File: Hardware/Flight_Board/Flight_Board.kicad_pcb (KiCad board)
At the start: 4 copper layers, 31.8 x 82.6 mm, 88 parts, among them J1 Conn_01x04, J2 Conn_01x08, J3 Conn_01x04, J4 Conn_01x06, J5 MEM2067-02-180-00-A_REVB, U1 FT5HN, U2 STM32F411RCTx, U3 ADXL375, U4 BMP390, U5 FGPMMOPA6H, U6 BMI323, U7 AP2205-33Y-13, U8 TPS274160A, U9 LR62E

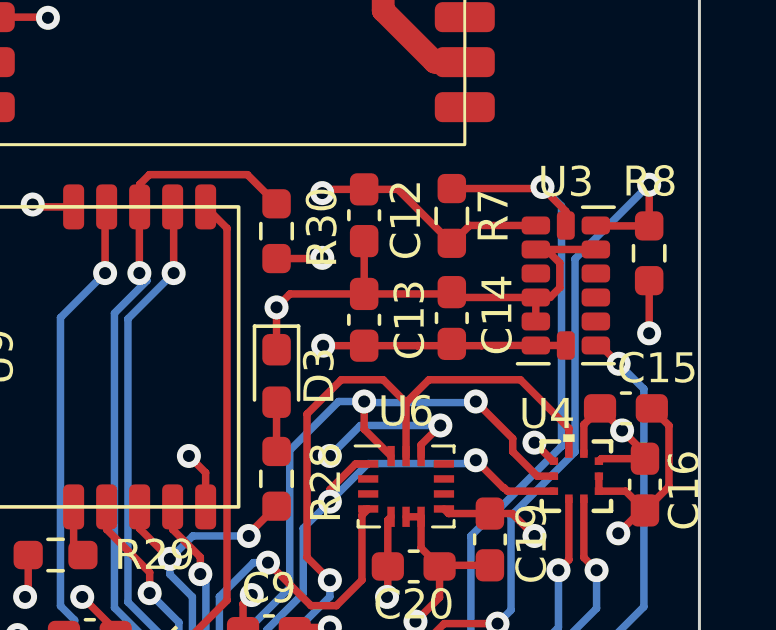
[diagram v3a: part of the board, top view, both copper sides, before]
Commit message: fix track stub and generate first gerbers
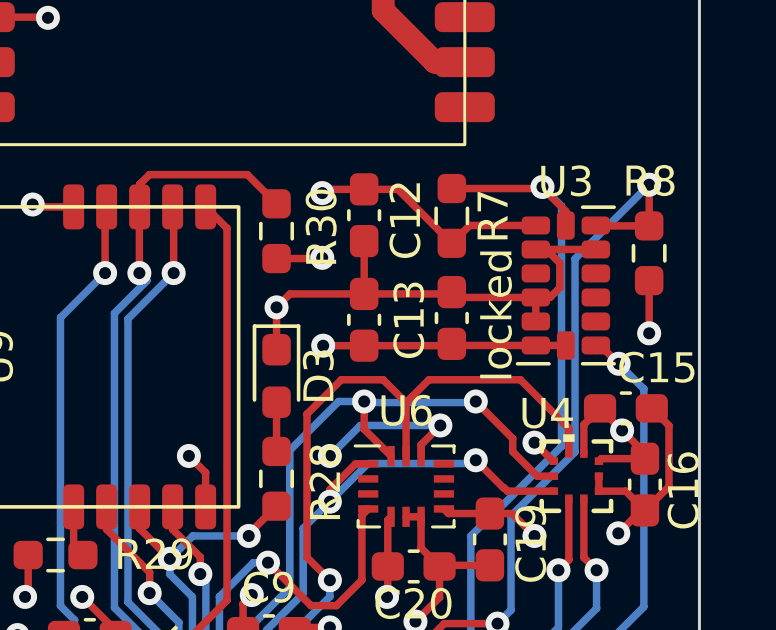
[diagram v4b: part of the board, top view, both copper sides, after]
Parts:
- renumbered C14 to locked
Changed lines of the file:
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@@
     (pad_to_mask_clearance 0)
     (pcbplotparams
-      (layerselection 0x00010fc_ffffffff)
+      (layerselection 0x00010f0_ffffffff)
       (plot_on_all_layers_selection 0x0000000_00000000)
       (disableapertmacros false)
-      (usegerberextensions false)
-      (usegerberattributes true)
+      (usegerberextensions true)
+      (usegerberattributes false)
       (usegerberadvancedattributes true)
       (creategerberjobfile true)
@@
       (plotinvisibletext false)
       (sketchpadsonfab false)
-      (subtractmaskfromsilk false)
+      (subtractmaskfromsilk true)
       (outputformat 1)
       (mirror false)
-      (drillshape 1)
+      (drillshape 0)
       (scaleselection 1)
-      (outputdirectory "")
+      (outputdirectory "gerbers")
     )
   )
@@
     (property "ki_keywords" "cap capacitor")
     (attr smd)
-    (fp_text reference "C14" (at 0.1005 1.524 90) (layer "F.SilkS")
+    (fp_text reference locked "C14" (at 0.1005 1.524 90) (layer "F.SilkS")
         (effects (font (size 1 1) (thickness 0.15)))
     )
@@
   (segment (start 148.1825 112.8988) (end 149.133819 111.947481) (width 0.25) (layer "F.Cu") (net 1))
   (segment (start 148.1825 115.062) (end 148.1825 115.9775) (width 0.25) (layer "F.Cu") (net 1))
+  (segment (start 160.073 86.995) (end 160.02 86.942) (width 0.25) (layer "F.Cu") (net 1))
   (segment (start 155.702 81.915) (end 155.826 81.791) (width 0.25) (layer "F.Cu") (net 1))
   (segment (start 155.826 81.791) (end 157.099 81.791) (width 0.25) (layer "F.Cu") (net 1))
@@
   (segment (start 151.815 92.376) (end 151.815 91.236) (width 0.25) (layer "F.Cu") (net 1))
   (segment (start 158.2155 107.7002) (end 158.2155 112.014) (width 0.25) (layer "F.Cu") (net 1))
+  (segment (start 160.02 86.942) (end 159.96 87.002) (width 0.25) (layer "F.Cu") (net 1))
   (segment (start 143.4835 108.405412) (end 143.4835 109.474) (width 0.25) (layer "F.Cu") (net 1))
   (segment (start 139.446 73.533) (end 138.684 74.295) (width 0.25) (layer "F.Cu") (net 1))
-  (segment (start 161.0095 87.002) (end 161.0165 86.995) (width 0.25) (layer "F.Cu") (net 1))
   (segment (start 164.423063 90.6017) (end 164.423063 89.629937) (width 0.25) (layer "F.Cu") (net 1))
   (segment (start 137.668 93.853) (end 137.541 93.726) (width 0.25) (layer "F.Cu") (net 1))
@@
   (segment (start 160.52525 137.493) (end 161.80075 137.493) (width 0.762) (layer "F.Cu") (net 1))
   (segment (start 163.83 122.301) (end 163.4725 122.6585) (width 0.25) (layer "F.Cu") (net 1))
-  (segment (start 158.8825 86.9965) (end 158.877 87.002) (width 0.25) (layer "F.Cu") (net 1))
   (segment (start 153.0615 95.605206) (end 153.0615 96.52) (width 0.25) (layer "F.Cu") (net 1))
-  (segment (start 158.877 87.002) (end 161.0095 87.002) (width 0.25) (layer "F.Cu") (net 1))
   (segment (start 161.29 92.5975) (end 159.912 92.5975) (width 0.25) (layer "F.Cu") (net 1))
   (segment (start 157.8875 94.361) (end 157.8875 95.3505) (width 0.25) (layer "F.Cu") (net 1))
@@
   (segment (start 153.352853 95.313853) (end 153.0615 95.605206) (width 0.25) (layer "F.Cu") (net 1))
   (segment (start 148.8175 98.3022) (end 149.133819 98.618519) (width 0.25) (layer "F.Cu") (net 1))
+  (segment (start 159.96 87.002) (end 157.099 87.002) (width 0.25) (layer "F.Cu") (net 1))
   (segment (start 154.2815 128.8815) (end 154.2815 128.27) (width 0.25) (layer "F.Cu") (net 1))
   (segment (start 159.766 122.428) (end 159.766 123.6715) (width 0.25) (layer "F.Cu") (net 1))
   (segment (start 153.416 115.7205) (end 150.114 115.7205) (width 0.25) (layer "F.Cu") (net 1))
   (segment (start 162.8155 87.0005) (end 162.821 86.995) (width 0.25) (layer "F.Cu") (net 1))
-  (segment (start 162.821 86.995) (end 161.0165 86.995) (width 0.25) (layer "F.Cu") (net 1))
   (segment (start 163.4725 122.6585) (end 163.4725 123.698) (width 0.25) (layer "F.Cu") (net 1))
   (segment (start 161.29 92.5975) (end 162.029 92.5975) (width 0.25) (layer "F.Cu") (net 1))
@@
   (segment (start 141.732 104.2905) (end 141.732 106.045) (width 0.25) (layer "F.Cu") (net 1))
   (segment (start 159.94075 136.9085) (end 160.52525 137.493) (width 0.762) (layer "F.Cu") (net 1))
+  (segment (start 162.821 86.995) (end 160.073 86.995) (width 0.25) (layer "F.Cu") (net 1))
   (segment (start 159.94075 136.9085) (end 159.3825 136.9085) (width 0.762) (layer "F.Cu") (net 1))
-  (segment (start 158.877 87.002) (end 157.099 87.002) (width 0.25) (layer "F.Cu") (net 1))
   (via (at 162.7765 93.345) (size 0.8) (drill 0.4) (layers "F.Cu" "B.Cu") (net 1))
   (via (at 155.7325 87.002) (size 0.8) (drill 0.4) (layers "F.Cu" "B.Cu") (net 1))

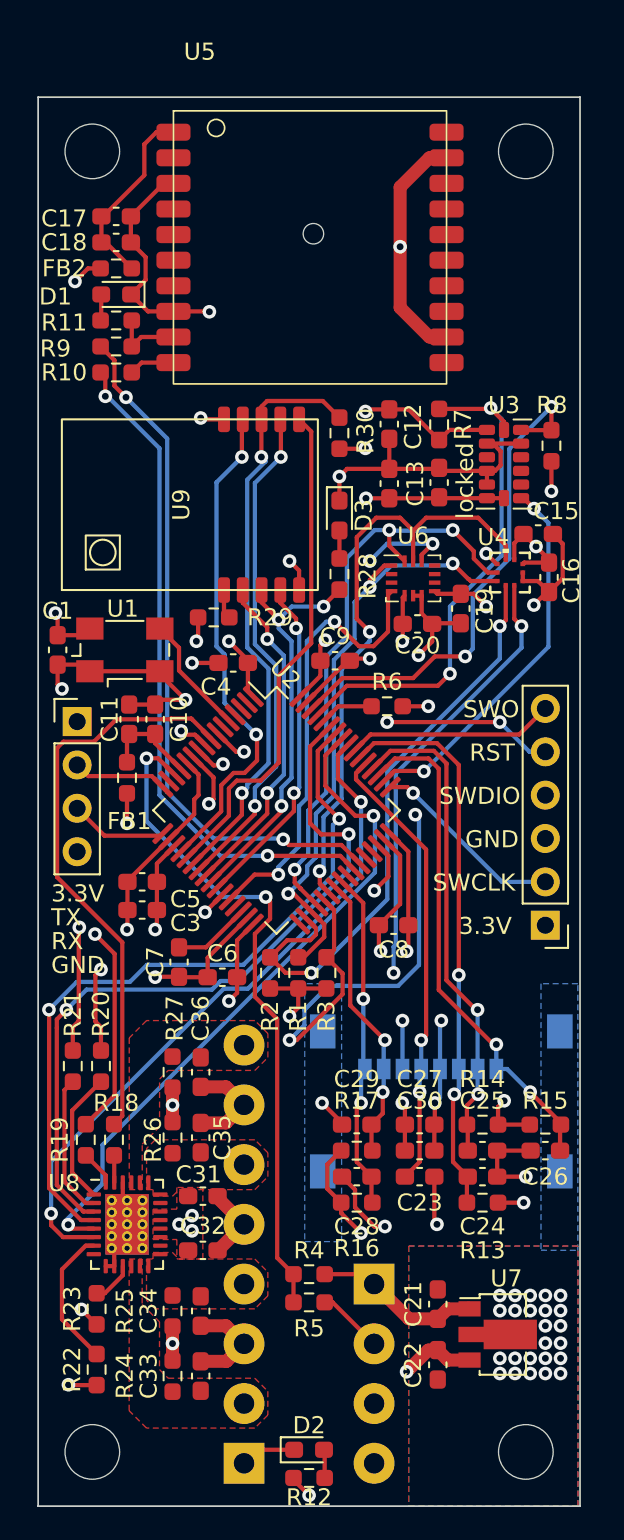
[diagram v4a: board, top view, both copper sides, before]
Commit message: reroute inner traces and tx/rx GPS lines
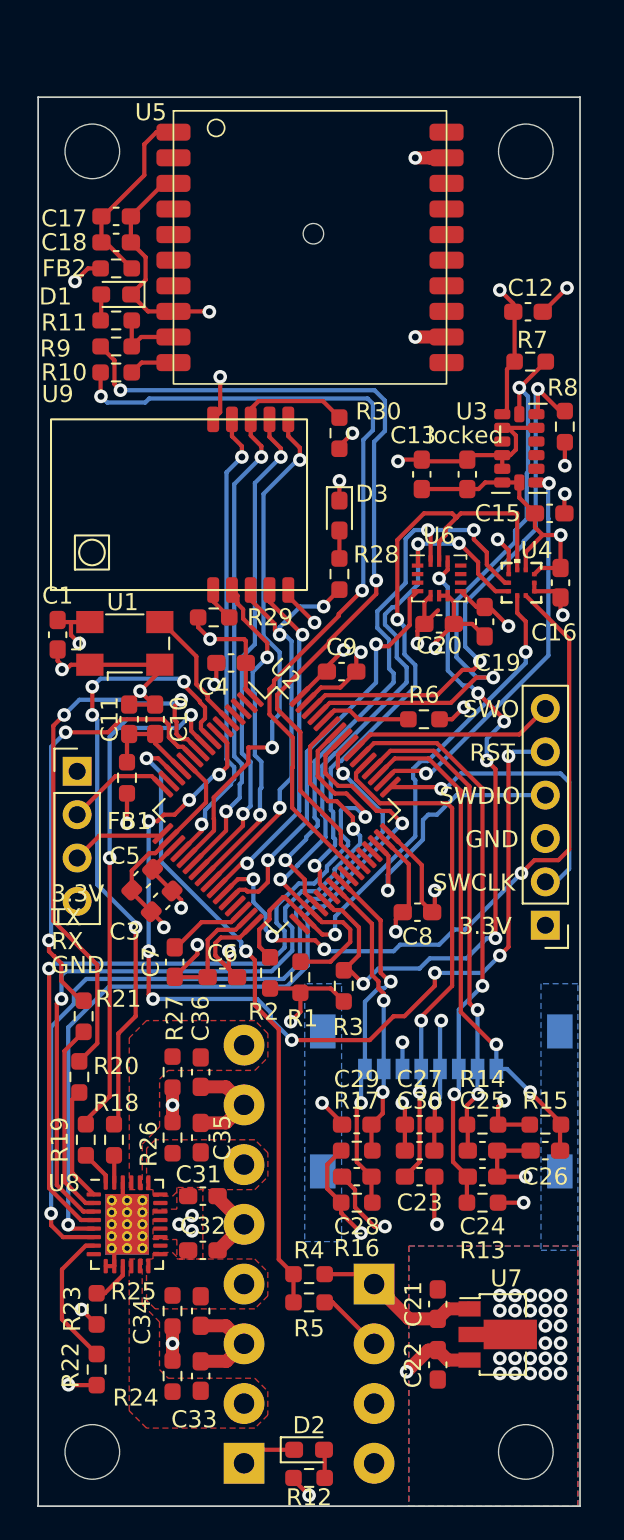
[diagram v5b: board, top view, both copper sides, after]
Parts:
- moved C12 10.5 mm to (165.2, 76.1), turned to 180 degrees
- moved R7 6.48 mm to (165.4, 79.0), turned to 0 degrees
- moved R21 2.99 mm to (139.2, 117.3)
- moved J3 2.91 mm to (138.8, 103.0)
- moved R6 2.29 mm to (159.1, 99.9)
- moved C13 1.98 mm to (159.0, 85.6)
- moved locked 1.72 mm to (161.7, 85.6)
- moved C19 1.60 mm to (162.7, 94.2)
- moved C8 1.59 mm to (158.8, 111.3)
- moved U6 1.52 mm to (160.0, 91.7)
- moved R20 1.42 mm to (138.9, 120.9)
- moved C15 1.38 mm to (166.5, 87.9)
- moved R8 1.37 mm to (167.4, 82.8)
- moved U3 1.29 mm to (164.7, 84.1)
- moved C20 1.27 mm to (160.0, 94.4)
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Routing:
- net /Microcontroller/NRST: track 21.1 -> 56.9 mm, vias 3 -> 9
- net GND: track 157.4 -> 143.7 mm, vias 46 -> 50
- net /Current Switch/EN3: track 22.2 -> 33.4 mm
- net /CS2: track 51.5 -> 40.7 mm, vias 4 -> 6
- net /GPS/RXD: track 39.5 -> 49.6 mm
- net /GPS/TXD: track 40.8 -> 50.8 mm
- net /Current Switch/~{ST3}: track 39.9 -> 47.9 mm
- net +3.3V: track 98.3 -> 106.1 mm, vias 26 -> 24
- net /Current Switch/~{ST4}: track 40.1 -> 47.7 mm
- net /Microcontroller/SWCLK: track 11.4 -> 18.5 mm
- net /Current Switch/~{ST2}: track 43.2 -> 49.9 mm
- net /Barometer/MISO: track 36.1 -> 42.1 mm
- net /Accelerometer/SCL: track 30.6 -> 35.3 mm
- net /Current Switch/EN4: track 22.3 -> 26.2 mm
- net /MicroSD/SDIO_CLK: track 26.7 -> 30.3 mm
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
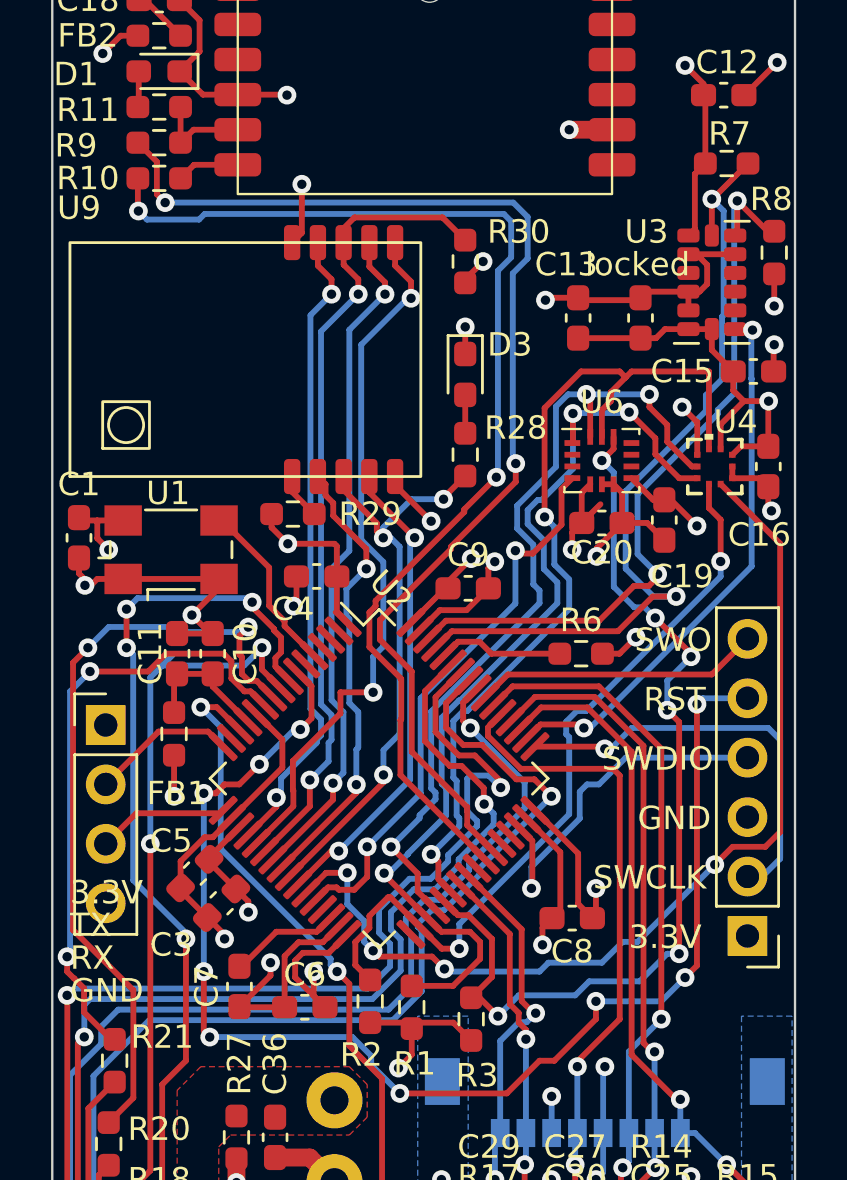
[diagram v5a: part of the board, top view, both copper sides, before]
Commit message: reroute floating traces in radio void
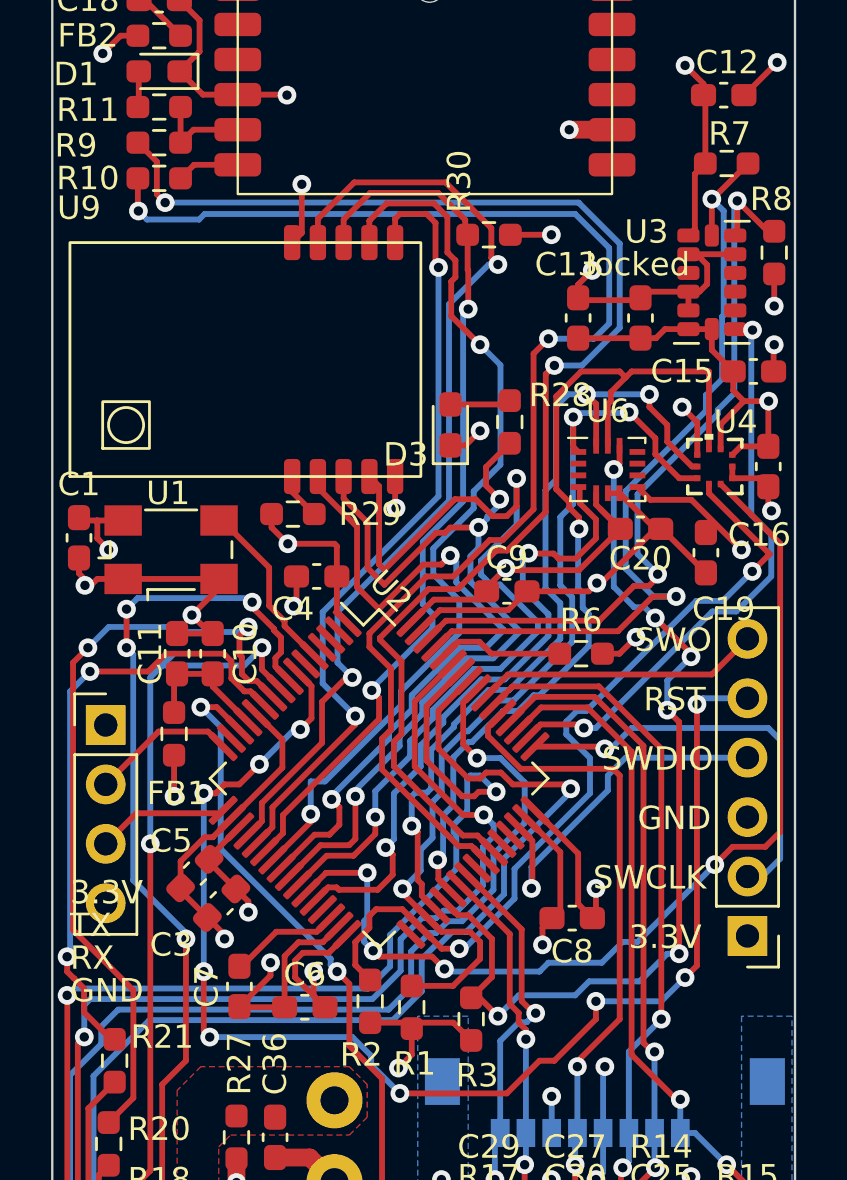
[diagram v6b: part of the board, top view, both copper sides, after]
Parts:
- moved R28 2.36 mm to (156.1, 90.0)
- moved C19 2.26 mm to (164.5, 95.6)
- moved D3 2.25 mm to (153.5, 90.2), turned to 90 degrees
- moved C20 1.67 mm to (161.7, 94.6)
- moved C9 1.66 mm to (156.0, 97.3)
- moved R30 1.53 mm to (155.2, 82.0), turned to 180 degrees
- moved U6 0.46 mm to (160.3, 92.1)
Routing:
- net /LoRa/LORA_DIO1: track 20.5 -> 37.7 mm
- net /LoRa/LORA_NSS: track 27.4 -> 41.3 mm
- net /LoRa/LORA_BUSY: track 25.1 -> 36.4 mm
- net /LoRa/LORA_RST: track 19.5 -> 30.3 mm
- net /LoRa/LORA_MOSI: track 29.1 -> 38.7 mm
- net /GPS/RXD: track 49.6 -> 57.6 mm
- net +3.3V: track 106.1 -> 113.2 mm, vias 24 -> 23
- net /GPS/TXD: track 50.8 -> 57.8 mm
- net GND: track 143.7 -> 150.7 mm, vias 50 -> 49
- net /LoRa/LORA_MISO: track 34.7 -> 38.6 mm
- net /IMU/INT1: track 24.1 -> 27.7 mm
- net /LoRa/LORA_SCK: track 30.5 -> 34.0 mm
- net /CS1: track 33.4 -> 36.2 mm
- net /Current Switch/~{ST3}: track 47.9 -> 50.4 mm
- net /Accelerometer/INT1: track 23.7 -> 25.1 mm
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
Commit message: create backpack board project and fix sikscreen
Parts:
- J3, J4: moved to B.Cu
- turned J3 to 180 degrees
- turned J4 to 0 degrees
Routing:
- net +3.3V: track 113.2 -> 112.0 mm
- net /Current Switch/EN2: track 31.5 -> 30.7 mm

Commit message: minor tweaks and prettification
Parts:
- added TP1: GND, TestPoint:TestPoint_Pad_D1.0mm, F.Cu at (167.0, 72.9)
- added TP10: SDA, TestPoint:TestPoint_Pad_D1.0mm, B.Cu at (167.5, 77.5)
- added TP11: SCL, TestPoint:TestPoint_Pad_D1.0mm, B.Cu at (163.2, 77.5)
- added TP15: SD_CLK, TestPoint:TestPoint_Pad_D1.0mm, F.Cu at (160.0, 119.0)
- added TP16: SD_CMD, TestPoint:TestPoint_Pad_D1.0mm, F.Cu at (163.8, 117.5)
- added TP17: SD_D0, TestPoint:TestPoint_Pad_D1.0mm, F.Cu at (157.5, 120.1)
- added TP2: GND, TestPoint:TestPoint_Pad_D1.0mm, B.Cu at (164.8, 73.4)
- added TP3: GND, TestPoint:TestPoint_Pad_D1.0mm, B.Cu at (159.8, 107.8)
- added TP4: GND, TestPoint:TestPoint_Pad_D1.0mm, F.Cu at (157.1, 85.0)
- added TP5: MISO, TestPoint:TestPoint_Pad_D1.0mm, B.Cu at (162.4, 90.3)
- added TP6: MOSI, TestPoint:TestPoint_Pad_D1.0mm, B.Cu at (163.3, 87.9)
- added TP7: SCK, TestPoint:TestPoint_Pad_D1.0mm, B.Cu at (159.6, 93.5)
- added TP8: CS1, TestPoint:TestPoint_Pad_D1.0mm, B.Cu at (155.8, 112.4)
- added TP9: CS2, TestPoint:TestPoint_Pad_D1.0mm, B.Cu at (160.3, 112.9)
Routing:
- net GND: track 150.7 -> 163.7 mm, vias 49 -> 40
- net /LoRa/LORA_RST: track 30.3 -> 23.7 mm
- net /LoRa/LORA_DIO1: track 37.7 -> 31.2 mm
- net /LoRa/LORA_BUSY: track 36.4 -> 30.5 mm
- net /Current Switch/~{ST2}: track 49.7 -> 45.9 mm
- net /Accelerometer/SDA: track 32.8 -> 36.6 mm
- net /Accelerometer/SCL: track 35.3 -> 38.9 mm
- net /MicroSD/SDIO_CMD: track 34.0 -> 36.4 mm
- net /MicroSD/SDIO_D0: track 16.9 -> 18.8 mm
- net /IMU/INT1: track 27.7 -> 25.7 mm
- net /Current Switch/~{ST1}: track 47.4 -> 45.5 mm
- net /MicroSD/SDIO_CLK: track 30.3 -> 32.1 mm
- net /CS1: track 36.2 -> 37.8 mm
- net /Current Switch/~{ST4}: track 48.2 -> 46.9 mm
- net /LoRa/LORA_MOSI: track 38.7 -> 37.6 mm
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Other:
- outline, holes or cut-outs redrawn
- board text added: "Rocket Flight Computer v1 2023/12/04 William Hutchinson RyLynd Bullington Ryan Parker Ethan Baranczuk"
- board text removed: "Rocket Flight Computer v1 William Hutchinson RyLynd Bullington Ryan Parker Ethan Baranczuk"
